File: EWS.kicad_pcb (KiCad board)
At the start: 4 copper layers, 65 x 56 mm, 108 parts, among them J301 GPIO, J401 PWR IN, J402 Toolhead 1, J403 Toolhead 2, J405 IN, J406 OUT, J407 OUT, Q401 CJAC70P06, Q403 AO3400A, Q404 CJAC70P06, Q405 AO3400A, SW301 RST, SW302 BOOT0, U201 XC6206PxxxMR, U202 XR76208, U301 STM32G0B1KBUx, U401 TJA1051TK-3, U402 CH334F, U403 USBLC6-2SC6, U404 USBLC6-2SC6, U405 USBLC6-2SC6

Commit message: Schema improvements and CAN transceiver modification
- Improved schema layout for better readability and organization
- Connected CAN transceiver S-pin to GND for proper operation
- Updated PCB layout to reflect schema changes
- Enhanced component placement and routing clarity
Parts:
- removed the REF** at (138.7, 93.5)
- removed the REF** at (135.9, 93.8)
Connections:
- net /Connectivity/CAN N renamed CAN L
- net /Connectivity/CAN P renamed CAN H
- net /Connectivity/HE GATE 1 renamed /Connectivity/HE1 GATE
- net /Connectivity/HE GATE 2 renamed /Connectivity/HE2 GATE
- net /Connectivity/VEXT renamed V_{EXT}
- net /MCU/SOC CAN RX renamed /MCU/SBC CAN RX
- net /MCU/SOC CAN TX renamed /MCU/SBC CAN TX
- net CAN_RX renamed Net-(JP306-C)
- net CAN_TX renamed Net-(JP301-C)
- C203 pad 2: 5VD -> 5V_{SYS}
- C401 pad 1: 5VD -> 5V_{SYS}
- C403 pad 2: 5V -> 5V_{SYS}
- C406 pad 1: /Connectivity/VBUS COUT -> Net-(U404-VBUS)
- D405 pad 1: 5VD -> 5V_{SYS}
- D406 pad 1: 5VD -> 5V_{SYS}
- F403 pad 1: 5V -> Net-(U404-VBUS)
- F403 pad 2: /Connectivity/VBUS COUT -> 5V
- J406 pad A4: /Connectivity/VBUS COUT -> Net-(U404-VBUS)
- J406 pad A9: /Connectivity/VBUS COUT -> Net-(U404-VBUS)
- J406 pad B4: /Connectivity/VBUS COUT -> Net-(U404-VBUS)
- J406 pad B9: /Connectivity/VBUS COUT -> Net-(U404-VBUS)
- R203 pad 1: 5V -> /Power/~{PGOOD}
- R203 pad 2: /Power/~{PGOOD} -> 5V
- R408 pad 2: 5VD -> 5V_{SYS}
- R409 pad 1: GND -> Net-(J405-CC1)
- R409 pad 2: Net-(J405-CC1) -> GND
- R410 pad 2: /Connectivity/VBUS COUT -> unconnected-(R410-Pad2)
- R411 pad 1: GND -> Net-(J405-CC2)
- R411 pad 2: Net-(J405-CC2) -> GND
- R412 pad 2: /Connectivity/VBUS COUT -> unconnected-(R412-Pad2)
- U201 pad 3: 5VD -> 5V_{SYS}
- U401 pad 3: 5V -> 5V_{SYS}
- U401 pad 8: unconnected-(U401-S-Pad8) -> GND
- U402 pad 19: 5VD -> 5V_{SYS}
- U404 pad 5: /Connectivity/VBUS COUT -> Net-(U404-VBUS)
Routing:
- net 5V_{SYS}: track 0.00 -> 40.6 mm, vias 0 -> 2
- net V_{EXT}: track 8.60 -> 25.7 mm
- net 5VD: track 12.1 -> 0.00 mm
- net /Connectivity/VBUS COUT: track 8.22 -> 0.00 mm, vias 22 -> 0
- net unconnected-(R412-Pad2): track 0.00 -> 4.11 mm
- net unconnected-(R410-Pad2): track 0.00 -> 4.11 mm
- net 5V: track 4.98 -> 2.79 mm, vias 75 -> 73
- net /Power/~{PGOOD}: track 2.99 -> 3.39 mm, vias 0 -> 1
- net Net-(U404-VBUS): vias 0 -> 22
- net GND: vias 187 -> 188
- added copper zone on B.Cu, net 5V
- removed copper zone on B.Cu, net /Connectivity/VBUS COUT
- removed copper zone on F.Cu, net /Connectivity/VBUS COUT

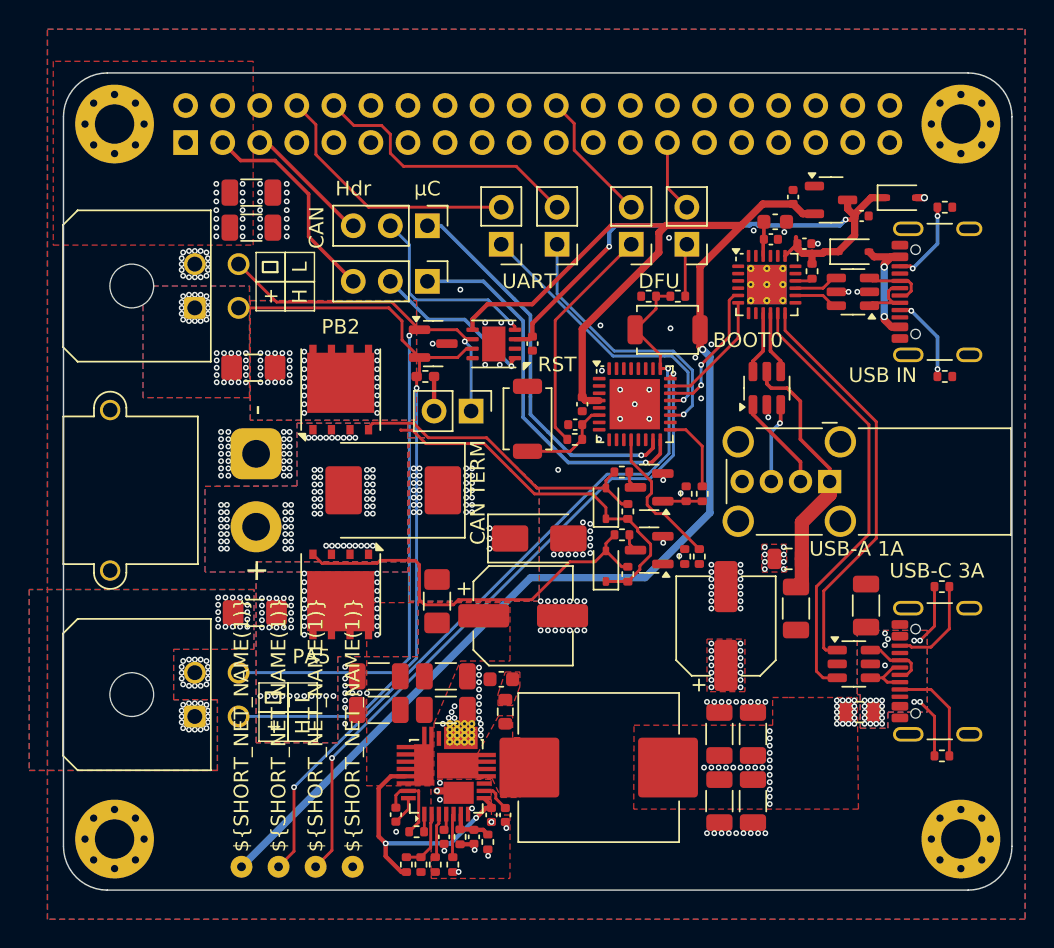
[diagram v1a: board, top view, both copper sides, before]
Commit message: Rev 0.2: Major hardware improvements and production readiness
Hardware Improvements (Thanks to shx for schematic cleanup):
- Clean up schematic organization and structure
- Set CAN transceiver Silent pin to GND for stability
- Add status LEDs (yellow: 24V/5V/3.3V, green: MCU PB4)
- Replace jumpers with solder jumpers on bottom side
- Add jumpers to output PFETs for permanent-on without firmware
- Add robust test points for 5V/GND load testing
- Add optional heatsink for DC/DC converter on bottom
- Add 10µF capacitor for MCU on 3.3V rail

Component Optimizations:
- Replace 30kΩ with 33kΩ basic part for simplified BOM
- Change DC/DC feedback: 15.5kΩ15kΩ (new output: 5.1V)
- Upgrade CAN ESD protection: NUP2105LPESD1CAN
- Increase CAN termination resistor footprint: 04020603
- Switch USB hub supply from 5V to 3.3V per datasheet

Production Ready:
- Add all LCSC part numbers and rotations
- Generate complete production data package
- Improve PCB layout and button placement
- Create comprehensive changelog documentation
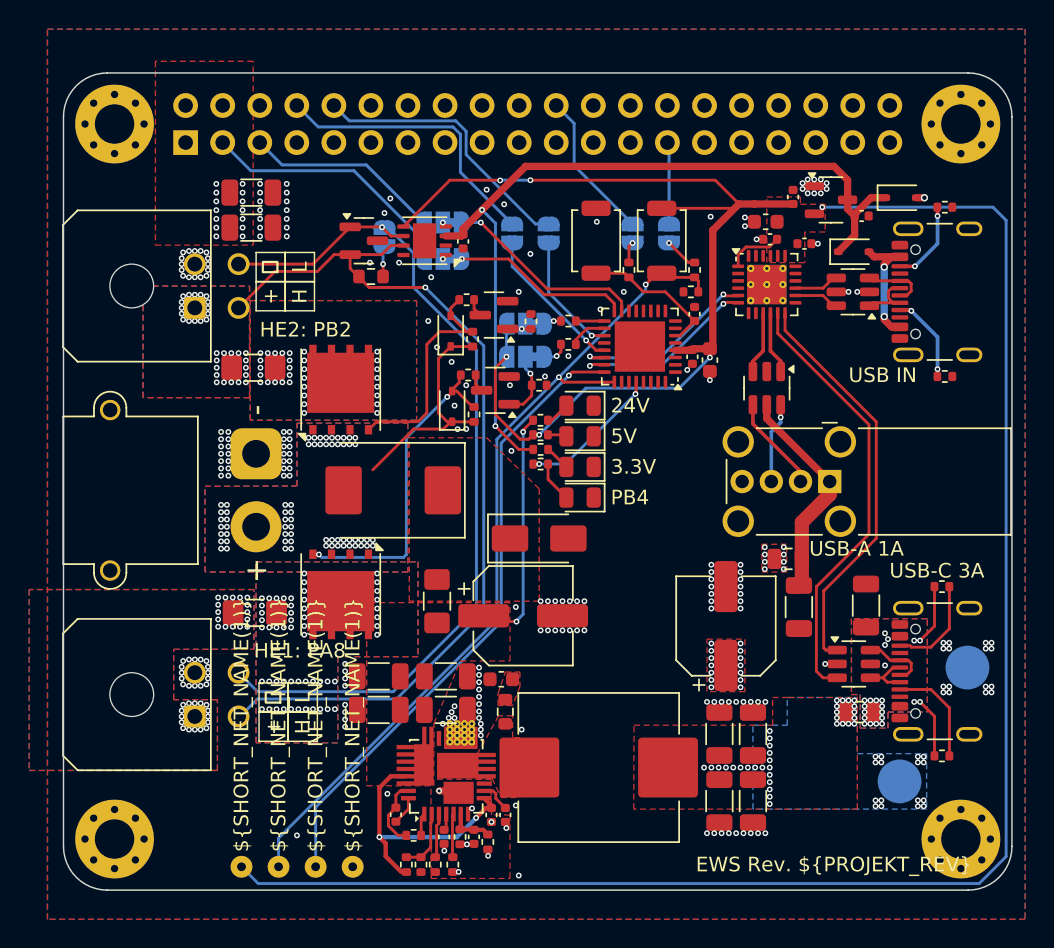
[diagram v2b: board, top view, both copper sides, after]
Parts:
- removed QR*****: http://github.com/eiten/EWS, project:http___github.com_eiten_EWS
- removed R416: 1k, Resistor_SMD:R_0402_1005Metric
- removed REF**: CC_BY_NC_SA 4, project:CC_BY_NC_SA 4
- removed REF**: HeatSink_9x9x5, project:HeatSink_9x9x5
- added C303: 10u, Capacitor_SMD:C_0603_1608Metric, F.Cu at (174.3, 86.7)
- added D201: YELLOW, LED_SMD:LED_0805_2012Metric, F.Cu at (165.4, 89.8)
- added D202: YELLOW, LED_SMD:LED_0805_2012Metric, F.Cu at (165.4, 94.0)
- added D203: YELLOW, LED_SMD:LED_0805_2012Metric, F.Cu at (165.4, 91.9)
- added D301: GREEN, LED_SMD:LED_0805_2012Metric, F.Cu at (165.4, 96.1)
- added HS201: Heatsink, project:HeatSink_9x9x5, B.Cu at (157.2, 112.2)
- added JP401: ~, project:SolderJumper-3_P1.3mm_Bridged12_RoundedPad1.0x1.5mm_custom, B.Cu at (161.7, 86.4)
- added JP402: ~, project:SolderJumper-3_P1.3mm_Bridged12_RoundedPad1.0x1.5mm_custom, B.Cu at (161.7, 84.2)
- added LABEL101: PCB NAME, project:EWS Rev. 1.0, B.Cu at (139.0, 98.0)
- added LABEL102: CREATED BY, project:EduardIten, B.Cu at (136.4, 98.5)
- added LABEL103: https://github.com/eiten/EWS, project:http___github.com_eiten_EWS, B.Cu at (174.5, 111.8)
- added LABEL104: LICENSE, project:CC_BY_NC_SA 4, B.Cu at (190.8, 100.8)
- added LABEL105: SWITZERLAND, project:Switzerland, B.Cu at (151.5, 94.7)
- added R201: 22k, Resistor_SMD:R_0402_1005Metric, F.Cu at (162.7, 90.8)
- added R202: 2k2, Resistor_SMD:R_0402_1005Metric, F.Cu at (162.7, 92.8)
- added R203: 1k, Resistor_SMD:R_0402_1005Metric, F.Cu at (162.7, 91.8)
- added R301: 330R, Resistor_SMD:R_0402_1005Metric, F.Cu at (162.7, 93.8)
- added TP202: 5V, TestPoint:TestPoint_Pad_D3.0mm, B.Cu at (187.3, 115.5)
- added TP203: GND, TestPoint:TestPoint_Pad_D3.0mm, B.Cu at (191.9, 107.8)
- D302: renamed from D404; value NUP2105L -> PESD1CAN
- D403: renamed from D402; value D_Schottky -> SS56
- J401: value PWR IN -> XT30
- J402: value Toolhead 1 -> MX3.0 2x2
- J403: value Toolhead 2 -> MX3.0 2x2
- J404: renamed from J405; value IN -> USB-C
- J405: renamed from J406; value OUT -> USB-C
- J406: renamed from J407; value OUT -> USB-A
- JP301: renamed from JP306; value Jumper_3_Open -> ~; footprint Connector_PinHeader_2.54mm:PinHeader_1x03_P2.54mm_Vertical -> project:SolderJumper-3_P1.3mm_Bridged12_RoundedPad1.0x1.5mm_custom; moved to B.Cu
- JP302: renamed from JP301; value Jumper_3_Open -> ~; footprint Connector_PinHeader_2.54mm:PinHeader_1x03_P2.54mm_Vertical -> project:SolderJumper-3_P1.3mm_Bridged12_RoundedPad1.0x1.5mm_custom; moved to B.Cu
- JP303: renamed from JP401; footprint Connector_PinHeader_2.54mm:PinHeader_1x02_P2.54mm_Vertical -> Jumper:SolderJumper-2_P1.3mm_Open_RoundedPad1.0x1.5mm; moved to B.Cu
- JP304: renamed from JP302; footprint Connector_PinHeader_2.54mm:PinHeader_1x02_P2.54mm_Vertical -> Jumper:SolderJumper-2_P1.3mm_Open_RoundedPad1.0x1.5mm; moved to B.Cu
- JP305: renamed from JP303; footprint Connector_PinHeader_2.54mm:PinHeader_1x02_P2.54mm_Vertical -> Jumper:SolderJumper-2_P1.3mm_Open_RoundedPad1.0x1.5mm; moved to B.Cu
- JP306: renamed from JP304; footprint Connector_PinHeader_2.54mm:PinHeader_1x02_P2.54mm_Vertical -> Jumper:SolderJumper-2_P1.3mm_Open_RoundedPad1.0x1.5mm; moved to B.Cu
- JP307: renamed from JP305; footprint Connector_PinHeader_2.54mm:PinHeader_1x02_P2.54mm_Vertical -> Jumper:SolderJumper-2_P1.3mm_Open_RoundedPad1.0x1.5mm; moved to B.Cu
- R207: renamed from R204; value 30k -> 33k
- R210: renamed from R207; value 15.5k -> 15k
- R304: renamed from R405; footprint Resistor_SMD:R_0402_1005Metric_Pad0.72x0.64mm_HandSolder -> Resistor_SMD:R_0603_1608Metric
- R401: renamed from R413; value 30k -> 33k
- R402: renamed from R401; value 30k -> 33k
- R403: renamed from R414; value 30k -> 33k
- R404: renamed from R403; value 30k -> 33k
- R405: renamed from R415; value 30k -> 33k
- R406: value 30k -> 33k
- SW301: value RST -> TS-1088
- SW302: value BOOT0 -> TS-1088
- U201: value XC6206PxxxMR -> XC6206P332MR
- moved R408 17.0 mm to (164.6, 84.0), turned to 180 degrees
- moved D402 15.9 mm to (156.5, 84.7)
- moved R402 15.9 mm to (158.0, 85.2)
- moved R406 15.9 mm to (162.0, 84.0)
- moved Q404 15.9 mm to (159.5, 83.6)
- moved R404 15.9 mm to (157.6, 82.5)
- moved R405 15.4 mm to (162.6, 88.4), turned to 180 degrees
- moved D401 15.2 mm to (156.6, 89.8)
- moved R401 15.2 mm to (158.1, 90.4)
- moved Q403 15.2 mm to (159.6, 88.8)
- moved R403 15.2 mm to (157.7, 87.7)
- moved R407 13.7 mm to (164.6, 85.6), turned to 180 degrees
- moved JP303 13.3 mm to (152.0, 78.2)
- moved SW301 13.1 mm to (166.5, 78.5)
- moved R302 12.2 mm to (168.8, 80.5), turned to -90 degrees
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- renumbered C403 to C304, C303 to C305, C304 to C306, C405 to C403, C406 to C405, C407 to C406, D407 to D401, D401 to D402, D403 to D404, Q404 to Q401, Q401 to Q402, Q405 to Q403, Q403 to Q404, R201 to R204, R202 to R205, R203 to R206, R205 to R208, R206 to R209, R208 to R211, R301 to R302, R302 to R303, R303 to R305, R411 to R410, R412 to R411, R410 to R412, TP302 to TP201, TP303 to TP302, TP304 to TP303, U401 to U301, U301 to U302, U402 to U401, U403 to U402, U404 to U403, U405 to U404
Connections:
- C401 pad 1: 5V_{SYS} -> 3V3
- C402 pad 1: Net-(U402-VDD33) -> 3V3
- C404 pad 1: Net-(U402-VDD33) -> 3V3
- C405 pad 1: Net-(U404-VBUS) -> Net-(U403-VBUS)
- F403 pad 1: Net-(U404-VBUS) -> 5V
- F403 pad 2: 5V -> Net-(U403-VBUS)
- J405 pad A4: Net-(U404-VBUS) -> Net-(U403-VBUS)
- J405 pad A9: Net-(U404-VBUS) -> Net-(U403-VBUS)
- J405 pad B4: Net-(U404-VBUS) -> Net-(U403-VBUS)
- J405 pad B9: Net-(U404-VBUS) -> Net-(U403-VBUS)
- J406 pad 2: Net-(J407-D-) -> Net-(J406-D-)
- J406 pad 3: Net-(J407-D+) -> Net-(J406-D+)
- Q404 pad 1: Net-(Q403-G) -> Net-(JP402-C)
- R206 pad 1: /Power/~{PGOOD} -> 5V
- R206 pad 2: 5V -> /Power/~{PGOOD}
- R406 pad 2: Net-(Q403-G) -> Net-(JP402-C)
- R407 pad 1: Net-(Q403-G) -> HE1 ON
- R407 pad 2: HE2 ON -> Net-(JP401-A)
- R408 pad 1: Net-(U402-~{RESET}) -> HE2 ON
- R408 pad 2: 5V_{SYS} -> Net-(JP402-A)
- R411 pad 2: unconnected-(R412-Pad2) -> Net-(U403-VBUS)
- R412 pad 2: unconnected-(R410-Pad2) -> Net-(U403-VBUS)
- U302 pad 12: HE1 ON -> unconnected-(U302-PA5-Pad12)
- U302 pad 18: unconnected-(U301-PA8-Pad18) -> HE1 ON
- U302 pad 28: unconnected-(U301-PB4-Pad28) -> Net-(U302-PB4)
- U401 pad 1: unconnected-(U402-~{OVCUR}-Pad1) -> 3V3
- U401 pad 10: /Connectivity/USB A DP -> /Connectivity/USB A DN
- U401 pad 16: Net-(U402-~{RESET}) -> unconnected-(U401-~{RESET}-Pad16)
- U401 pad 18: GND -> unconnected-(U401-PSELF-Pad18)
- U401 pad 19: 5V_{SYS} -> 3V3
- U401 pad 20: (no net) -> 3V3
- U401 pad 22: Net-(U402-VDD33) -> unconnected-(U401-LED1-Pad22)
- U401 pad 9: /Connectivity/USB A DN -> /Connectivity/USB A DP
- U403 pad 5: Net-(U404-VBUS) -> Net-(U403-VBUS)
- U404 pad 1: Net-(J407-D-) -> /Connectivity/USB A DN
- U404 pad 3: Net-(J407-D+) -> /Connectivity/USB A DP
- U404 pad 4: /Connectivity/USB A DP -> Net-(J406-D-)
- U404 pad 6: /Connectivity/USB A DN -> Net-(J406-D+)
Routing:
- net 3V3: track 106.4 -> 186.5 mm, vias 1 -> 6
- net /Power/VIN: track 18.0 -> 34.9 mm, vias 2 -> 4
- net 5V_{SYS}: track 40.6 -> 56.9 mm
- net Net-(JP304-A): track 15.9 -> 1.44 mm, vias 0 -> 1
- net /MCU/uC FDCAN1 TX: track 26.2 -> 12.2 mm
- net Net-(JP301-C): track 13.6 -> 0.36 mm
- net /MCU/uC FDCAN1 RX: track 26.7 -> 13.8 mm
- net Net-(JP302-C): track 11.4 -> 0.36 mm
- net /MCU/uC USART TX: track 19.0 -> 8.43 mm
- net CAN H: track 53.0 -> 63.3 mm
- net V_{EXT}: track 25.7 -> 15.7 mm, vias 74 -> 64
- net Net-(U302-PB4): track 0.00 -> 9.83 mm, vias 0 -> 2
- net /MCU/uC USART RX: track 19.4 -> 10.3 mm
- net Net-(U403-VBUS): track 0.00 -> 8.22 mm, vias 0 -> 22
- net HE1 ON: track 10.0 -> 2.60 mm
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- added copper zone on F.Cu, net 3V3
- added copper zone on B.Cu, net Net-(U403-VBUS)
- added copper zone on F.Cu, net Net-(U403-VBUS)
- removed copper zone on B.Cu, net 24V
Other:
- board text added: "24V"
- board text added: "3.3V"
- board text added: "5V"
- board text added: "EWS Rev. ${PROJEKT_REV}"
- board text added: "HE1"
- board text added: "HE1: PA8"
- board text added: "HE2"
- board text added: "HE2: PB2"
- board text added: "ON"
- board text added: "PB4"
- board text added: "SBC"
- board text added: "TERM 120Ω"
- board text added: "~{RST}"
- board text removed: "CAN TERM"
- board text removed: "Hdr"
- board text removed: "PA5"
- board text removed: "PB2"
- board text removed: "RST"
